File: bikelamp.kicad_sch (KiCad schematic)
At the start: 26 parts, among them J1 Conn_ARM_SWD_TagConnect_TC203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, J2 Conn_01x04_Pin, Q1 Q_PMOS_GSD, Q2 BSS138, SW1 SW_MEC_5E, U1 MCP79402T-xSN, U3 MIC5205-3.3YM5, U4 MMA8452QR1, U5 YJ-14015, U6 MC-306

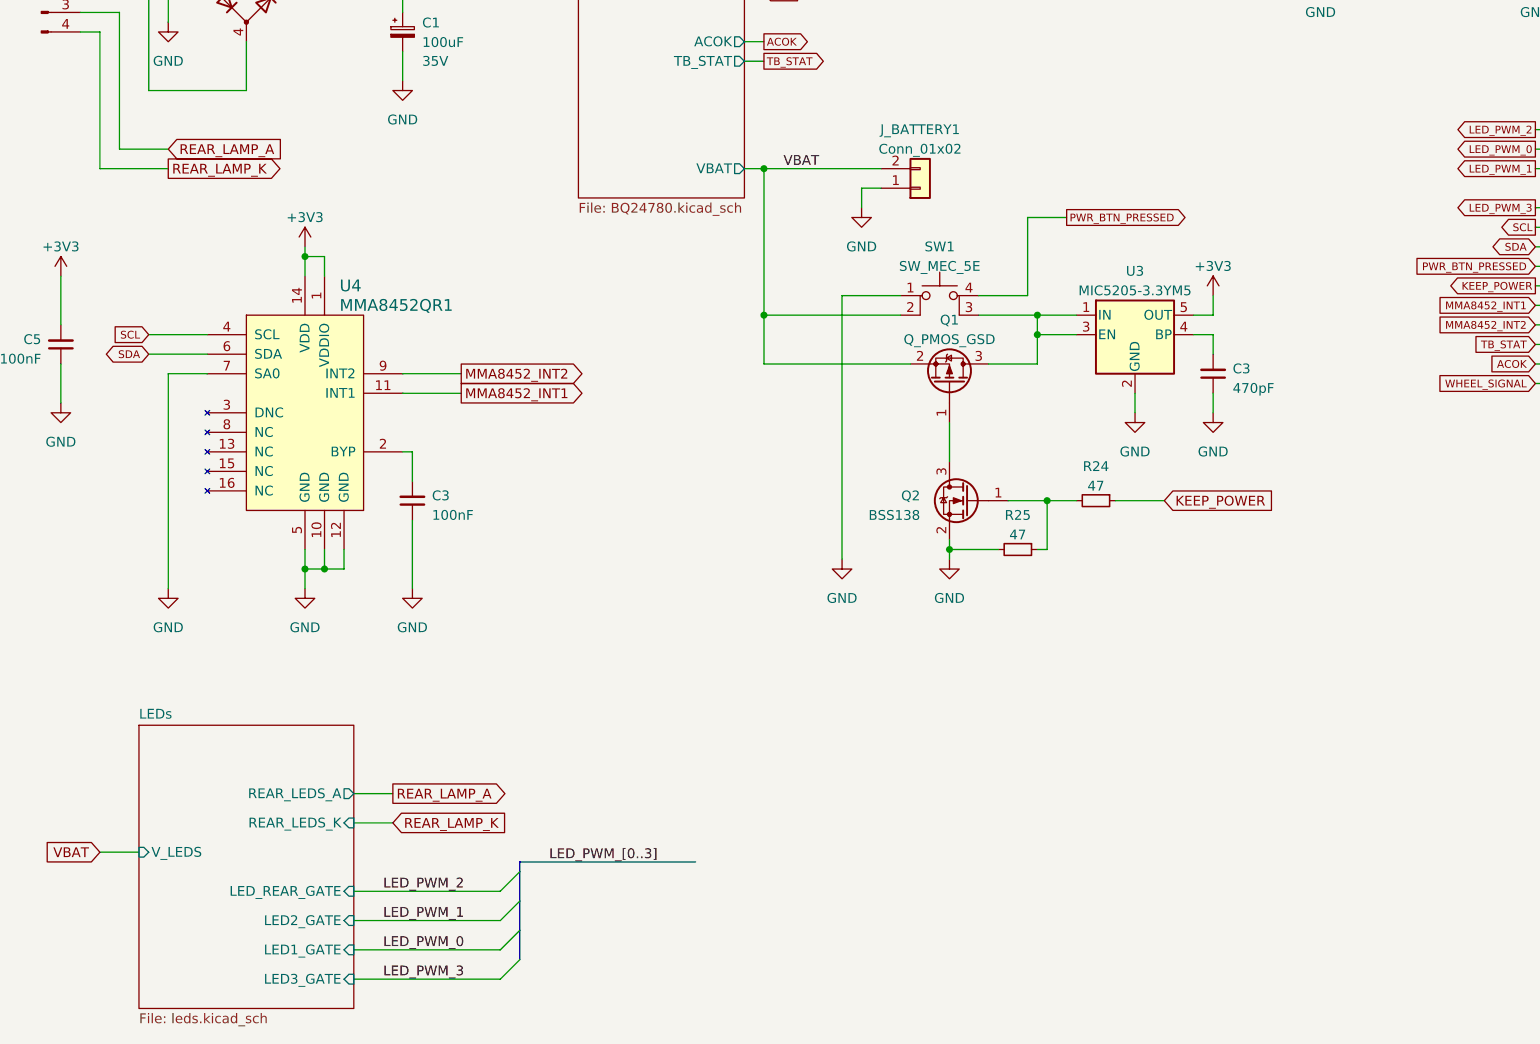
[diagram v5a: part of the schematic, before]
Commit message: - Get rid from <0.3 mm drills - Fine tune GND fill
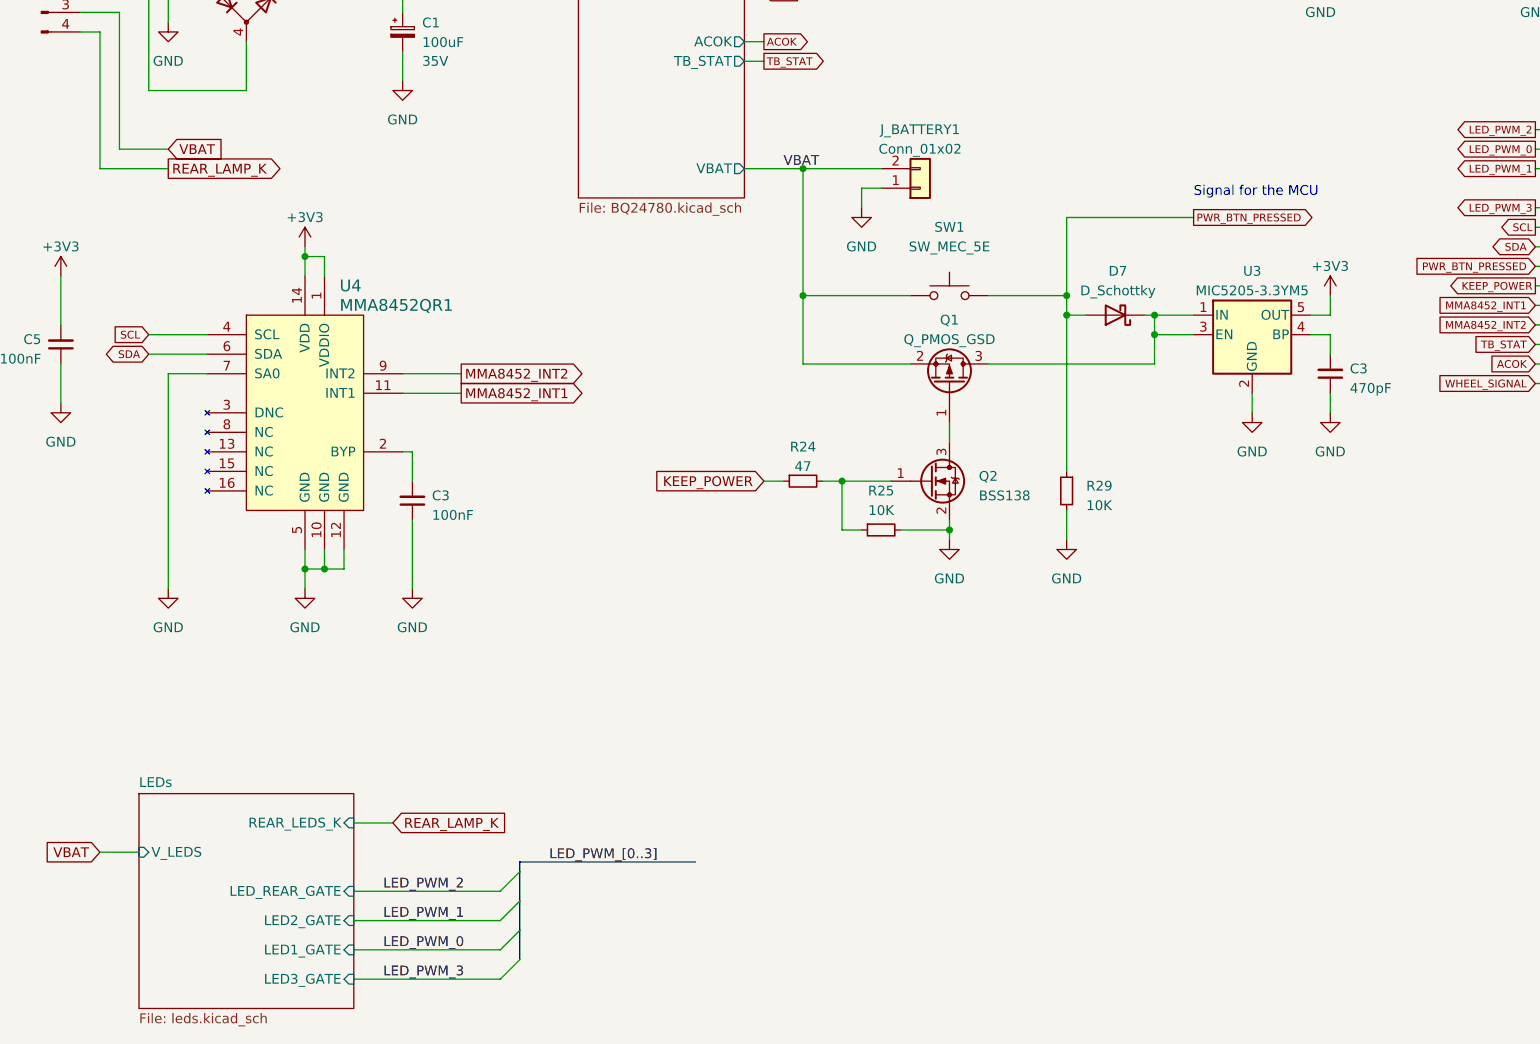
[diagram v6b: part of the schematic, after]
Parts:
- added D7: D_Schottky, Diode_SMD:D_MicroMELF, symbol Device:D_Schottky
- added R29: 10K, Resistor_SMD:R_0603_1608Metric, symbol Device:R_Small
- R25: value 47 -> 10K
- SW1: symbol Switch:SW_MEC_5E -> Switch:SW_Push
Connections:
- net REAR_LAMP_A is gone; now on net VBAT: J2.3 (Pin_3)
- net GND: now also R29.2; no longer SW1.1
- net PWR_BTN_PRESSED: now also SW1.1, D7.2 (A), R29.1; no longer SW1.4 (A)
- net at Q1.3 (D), U3.1 (IN), U3.3 (EN): now also D7.1 (K); no longer SW1.3 (K)
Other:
- sheet LEDs ports: added none; removed REAR_LEDS_A
- note added: "Signal for the MCU"
- moved on the sheet: C3, Q2, R24, R25, U3
